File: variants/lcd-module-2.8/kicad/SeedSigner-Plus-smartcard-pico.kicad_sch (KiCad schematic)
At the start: 0 parts

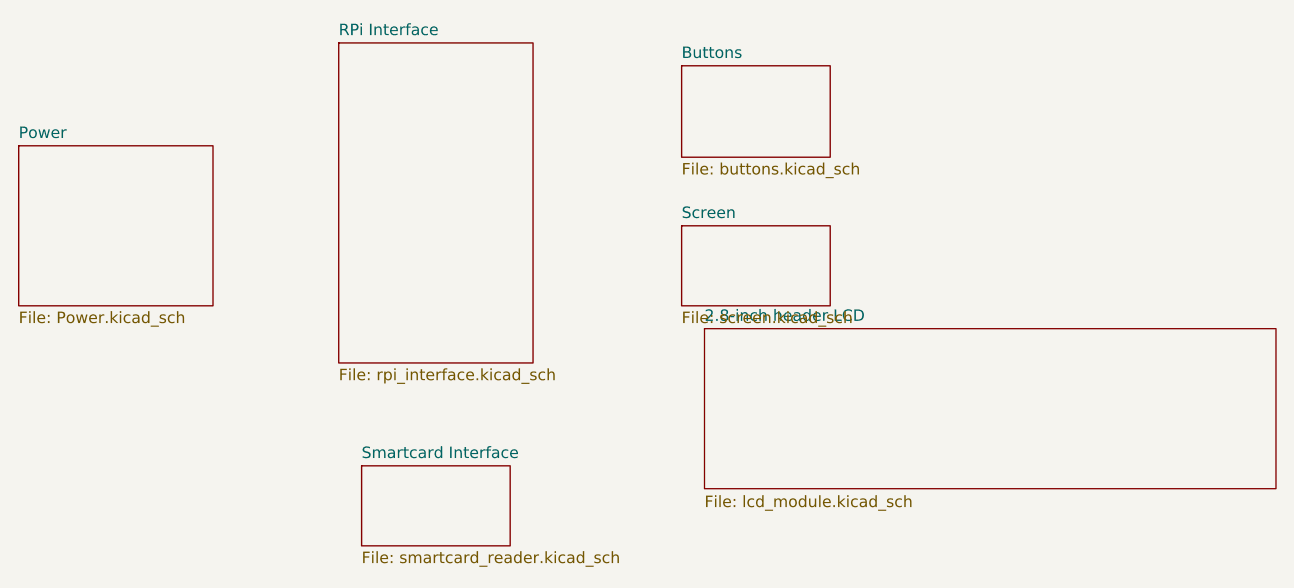
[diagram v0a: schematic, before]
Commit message: Rebuild modular signer as an eight-pin 2.8-inch pill carrier
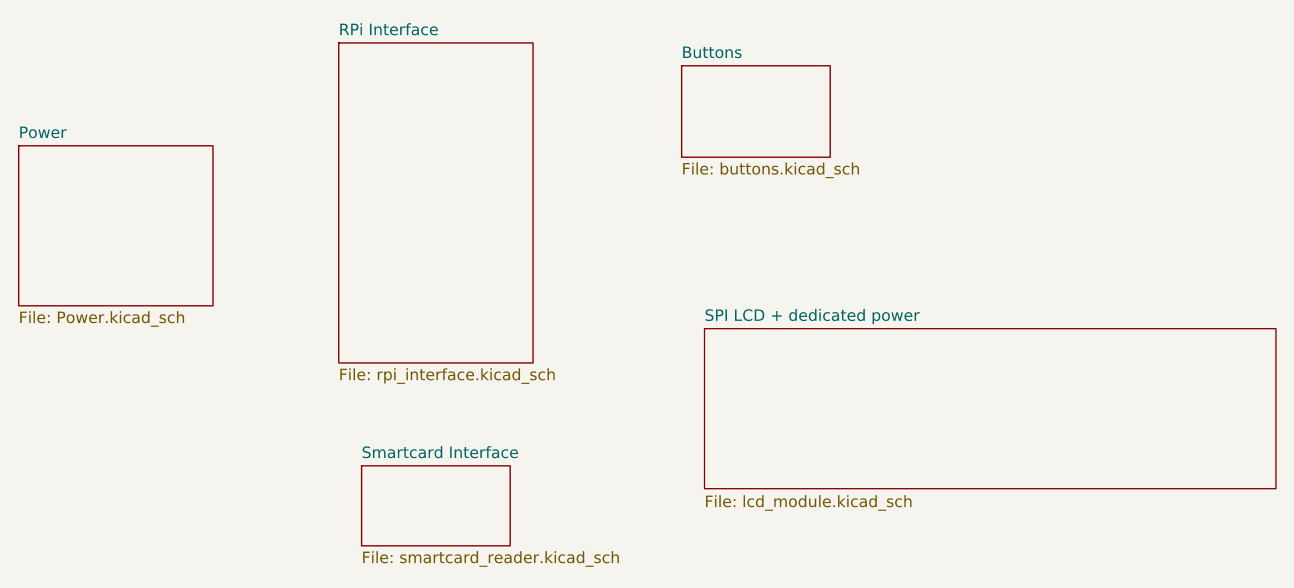
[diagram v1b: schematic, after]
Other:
- sheet 2.8-inch header LCD renamed SPI LCD + dedicated power
- removed sheet Screen
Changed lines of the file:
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@@
 			(project "SeedSigner-Plus-smartcard-pico"
 				(path "/8c9c54c8-0cfa-43ef-b1ba-3cda1bca877f"
-					(page "6")
-				)
-			)
-		)
-	)
-	(sheet
-		(at 187.96 88.9)
-		(size 16.51 8.89)
-		(exclude_from_sim no)
-		(in_bom yes)
-		(on_board yes)
-		(dnp no)
-		(fields_autoplaced yes)
-		(stroke
-			(width 0.1524)
-			(type solid)
-		)
-		(fill
-			(color 0 0 0 0)
-		)
-		(property "Sheetname" "Screen"
-			(at 187.96 88.1884 0)
-			(show_name no)
-			(do_not_autoplace no)
-			(effects
-				(font
-					(size 1.27 1.27)
-				)
-				(justify left bottom)
-			)
-		)
-		(property "Sheetfile" "screen.kicad_sch"
-			(at 187.96 98.3746 0)
-			(show_name no)
-			(do_not_autoplace no)
-			(effects
-				(font
-					(size 1.27 1.27)
-				)
-				(justify left top)
-			)
-		)
-		(instances
-			(project "SeedSigner-Plus-smartcard-pico"
-				(path "/8c9c54c8-0cfa-43ef-b1ba-3cda1bca877f"
-					(page "4")
+					(page "5")
 				)
 			)
@@
 			(project "SeedSigner-Plus-smartcard-pico"
 				(path "/8c9c54c8-0cfa-43ef-b1ba-3cda1bca877f"
-					(page "5")
+					(page "4")
 				)
 			)
@@
 (sheet (at 190.5 100.33) (size 63.5 17.78) (fields_autoplaced yes)
       (stroke (width 0) (type default)) (fill (color 0 0 0 0))
-      (property "Sheetname" "2.8-inch header LCD" (at 190.5 99.6184 0) (effects (font (size 1.27 1.27)) (justify left bottom)))
+      (property "Sheetname" "SPI LCD + dedicated power" (at 190.5 99.6184 0) (effects (font (size 1.27 1.27)) (justify left bottom)))
       (property "Sheetfile" "lcd_module.kicad_sch" (at 190.5 118.8216 0) (effects (font (size 1.27 1.27)) (justify left top)))
-      (instances (project "SeedSigner-Plus-smartcard-pico" (path "/8c9c54c8-0cfa-43ef-b1ba-3cda1bca877f" (page "7")))))
+      (instances (project "SeedSigner-Plus-smartcard-pico" (path "/8c9c54c8-0cfa-43ef-b1ba-3cda1bca877f" (page "6")))))
 )
